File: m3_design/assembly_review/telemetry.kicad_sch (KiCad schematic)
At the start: 37 parts, among them J130 RADIO M0/M1/RXD/TXD/AUX/VCC/G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, J131 GPS 5V/GND/TX/RX, U14 AP63301WU-7, U15 TPS2553DBVR, U16 TPS259570DSGR

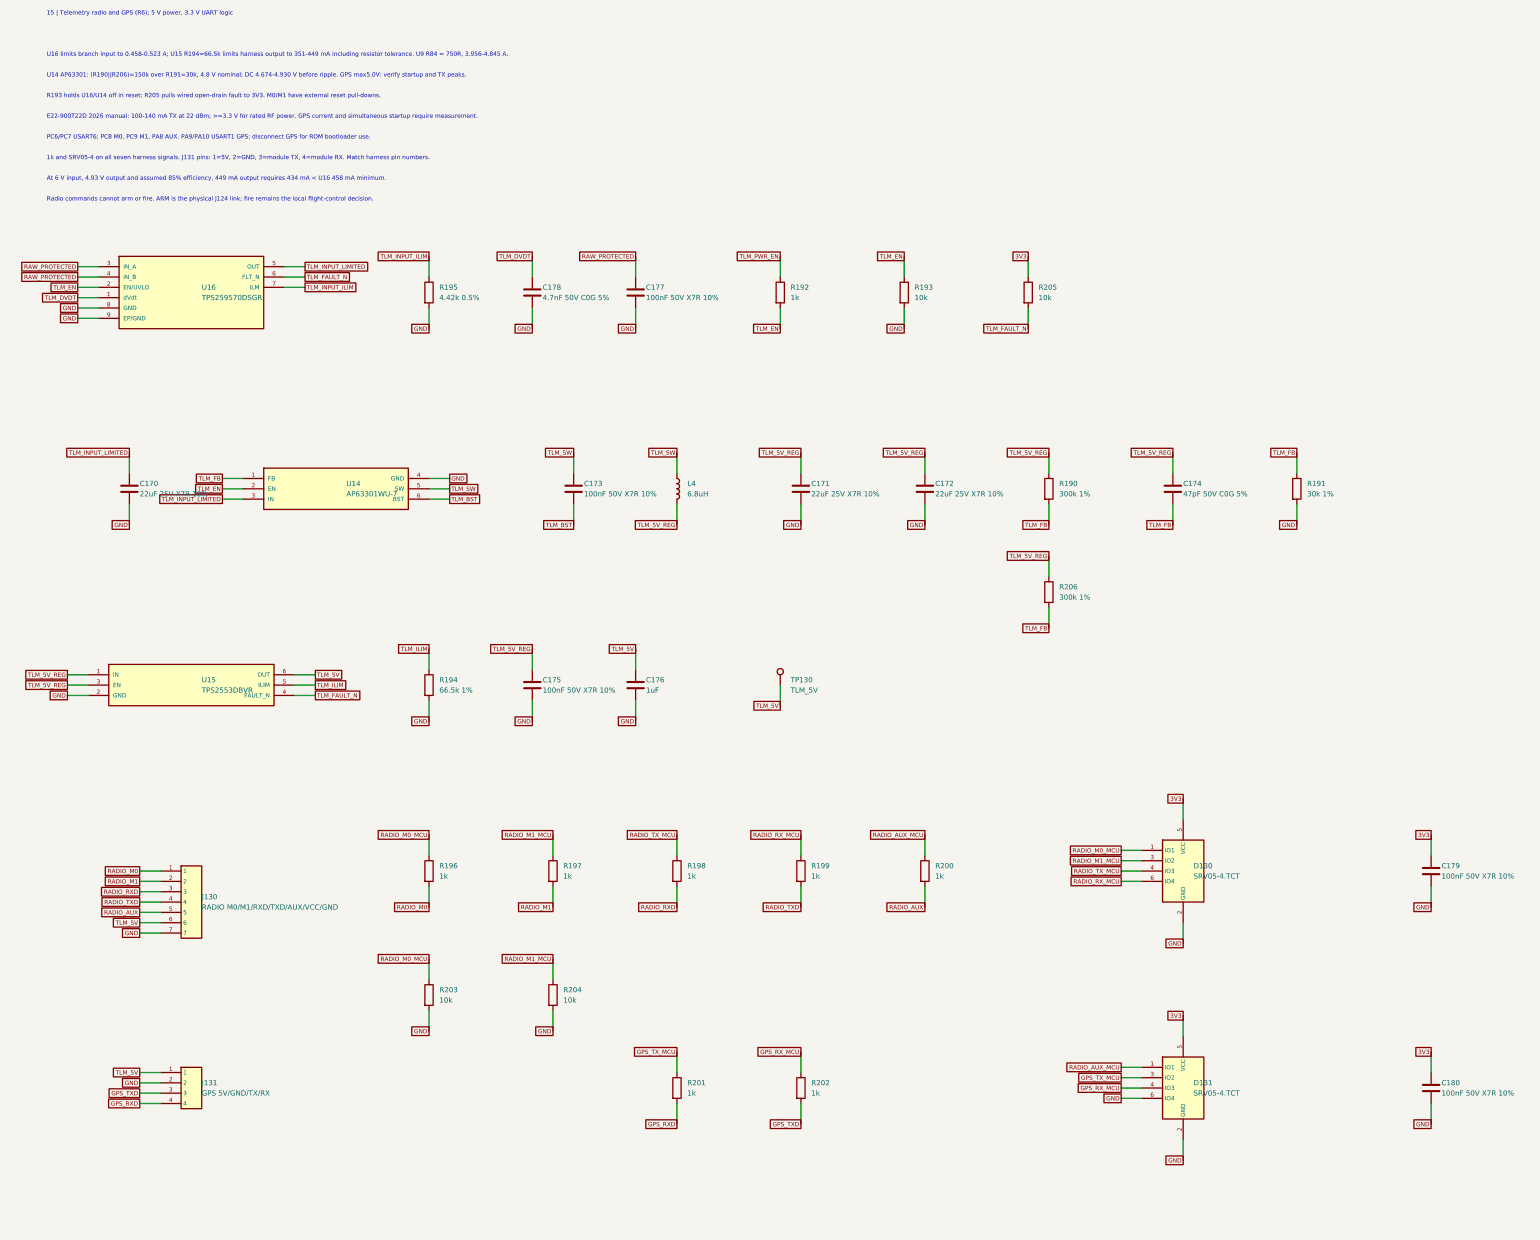
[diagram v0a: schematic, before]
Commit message: M3-ASSY-R7: on-board GNSS and LoRa radio, clean-routing gate, owner-accepted deviations
R7 replaces R6's external radio/GPS harness ports with an on-board u-blox
MAX-F10S (U30, MAX-M10S drop-in) and EBYTE E22-900MM22S SX1262 radio (U31)
in an RF strip at the aft end, each with an edge-launch SMA jack (J30 GNSS,
J31 RADIO), RF ESD, an antenna-bias current limiter and DNP tuning pads.
The board grows to 46 x 118 mm (R6 copper translated +18 mm).

- Schematic, parts and footprints: r7_sch.py, r7_parts.py
- Reproducible board build from the SHA-checked R6 board: r7_build.sh
  (r7_pcb, r7_route, r7_redraw, r7_rework, r7_hygiene, r7_polish, r7_post)
- Gate: check_r7.py (RF contract), route_check.py (clean routing, M2)
  in tools/check.sh; fit_check, cost and procurement updated for R7
- Eight independent review passes with skeptic verification; pass 8 on
  this board found 0 Critical / 0 Major
- Owner accepted the deviation list on 2026-10-18 (R7_VALIDATION), with
  the 7.7 A servo-feed copper rise accepted as estimated

Board SHA-256 c872a3d30509cccf5f78b64cde48ef722ee85c7be23c4848b07ce4082a852de3.
tools/check.sh: DRC 0, unconnected 0, parity 0, ERC 0; audit, silk,
R7 contract, routing hygiene (0 failing), actuator contract and fit OK.
Before ordering: consign U4 and get JLC's forward-rail confirmation.

Co-Authored-By: Claude Opus 5.5 <noreply@anthropic.com>
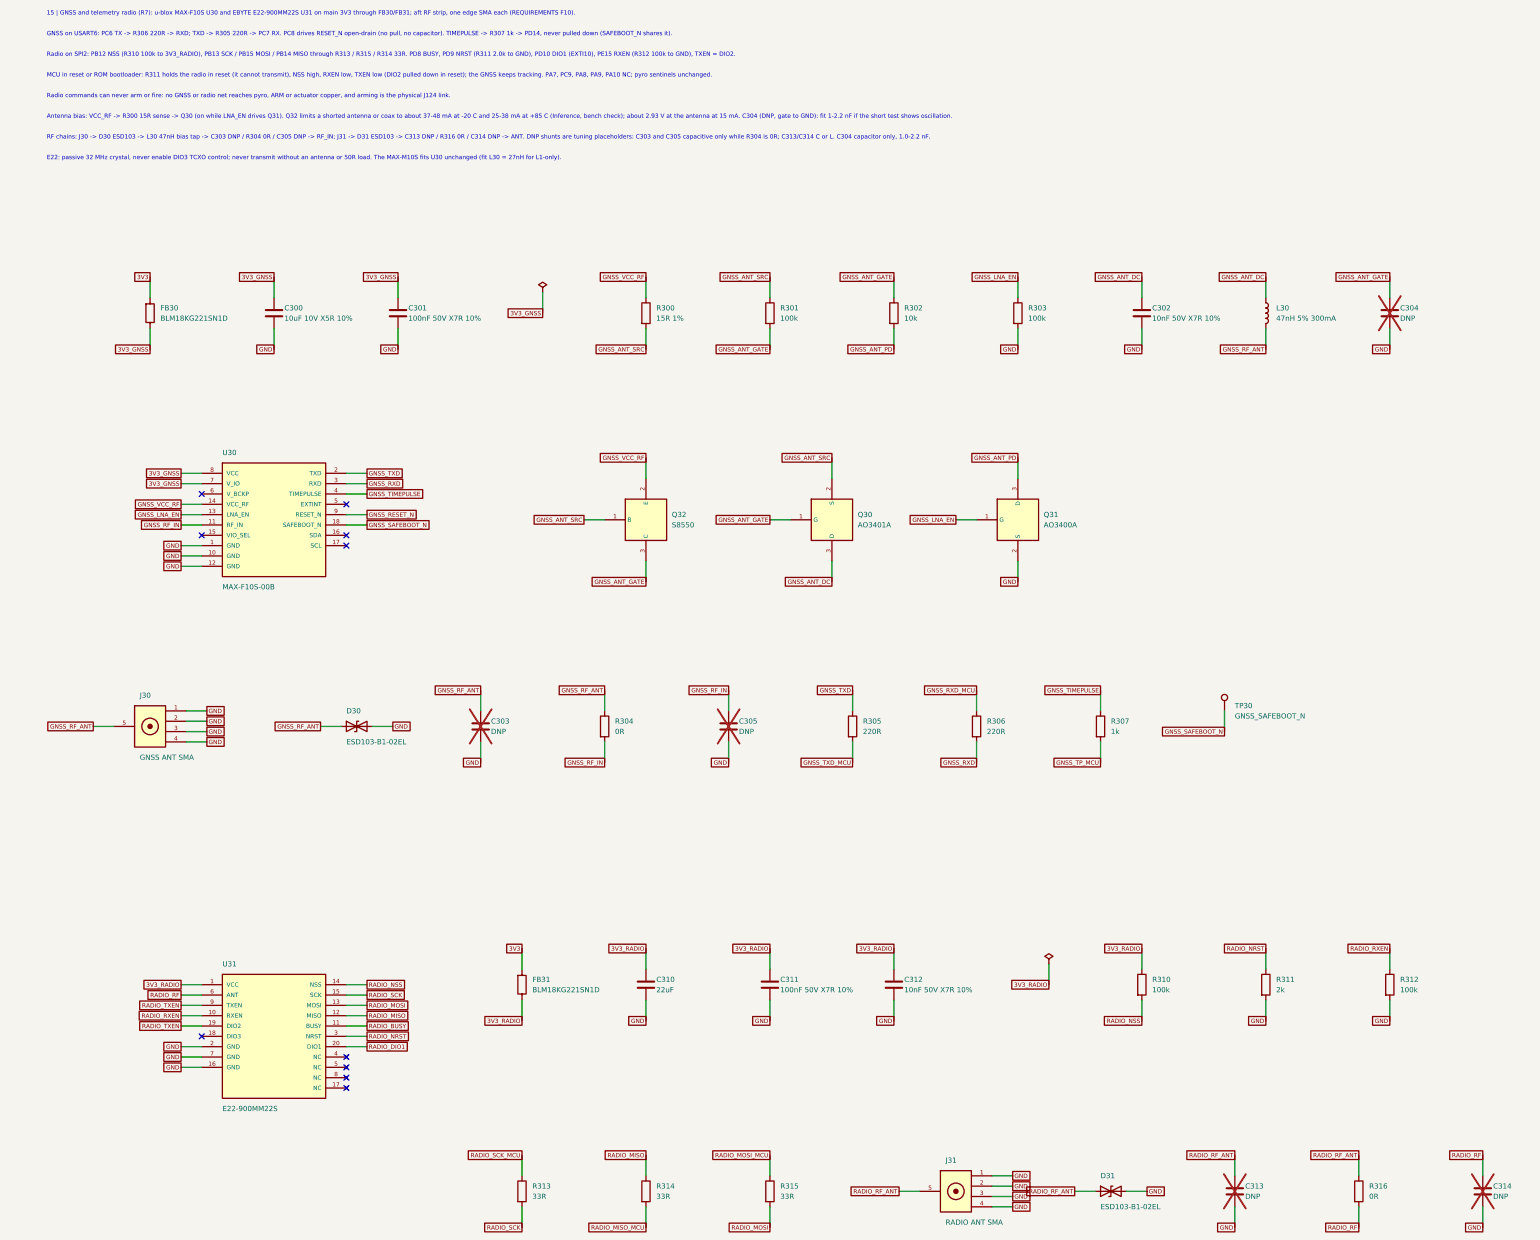
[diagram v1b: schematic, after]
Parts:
- removed C170, C171, C172: 22uF 25V X7R 10%, rocket:M3_GRM32_1210, symbol M3:C
- removed C173, C175, C177, C179, C180: 100nF 50V X7R 10%, rocket:C_0603_1608Metric, symbol M3:C
- removed C174: 47pF 50V C0G 5%, rocket:C_0603_1608Metric, symbol M3:C
- removed C176: 1uF, rocket:C0603, symbol M3:C
- removed C178: 4.7nF 50V C0G 5%, rocket:C_0603_1608Metric, symbol M3:C
- removed D130, D131: SRV05-4.TCT, rocket:SOT-23-6_L2.9-W1.6-P0.95-LS2.8-BL, symbol M3:SRV05_4
- removed J130: RADIO M0/M1/RXD/TXD/AUX/VCC/GND, rocket:M3_SH_BM07B_SRSS_TB, symbol M3:Conn_1x7
- removed J131: GPS 5V/GND/TX/RX, rocket:M3_SH_BM04B_SRSS_TB, symbol M3:Conn_1x4
- removed L4: 6.8uH, rocket:M3_SRP5030TA, symbol M3:L
- removed R190, R206: 300k 1%, rocket:R_0603_1608Metric, symbol M3:R
- removed R191: 30k 1%, rocket:R_0603_1608Metric, symbol M3:R
- removed R192, R196, R197, R198, R199, R200, R201, R202: 1k, rocket:R0402, symbol M3:R
- removed R193, R203, R204, R205: 10k, rocket:R0402, symbol M3:R
- removed R194: 66.5k 1%, rocket:R_0603_1608Metric, symbol M3:R
- removed R195: 4.42k 0.5%, rocket:R_0603_1608Metric, symbol M3:R
- removed TP130: TLM_5V, rocket:M3_TestPad_1.5, symbol M3:TestPoint
- removed U14: AP63301WU-7, rocket:M3_AP63200_TSOT26, symbol M3:CameraBuck
- removed U15: TPS2553DBVR, rocket:M3_TPS2553_DBV, symbol M3:USBCurrentLimit
- removed U16: TPS259570DSGR, rocket:M3_TPS2595_DSG, symbol M3:CameraEFuse
- added C300: 10uF 10V X5R 10%, rocket:C0603, symbol M3:C
- added C301, C311: 100nF 50V X7R 10%, rocket:C0402, symbol M3:C
- added C302, C312: 10nF 50V X7R 10%, rocket:C0402, symbol M3:C
- added C303, C304, C305, C313, C314: DNP, rocket:C0402_DNP, symbol M3:C
- added C310: 22uF, rocket:C0805, symbol M3:C
- added D30, D31: ESD103-B1-02EL, rocket:M3_TSLP_2_20, symbol M3:ESD_Bidir
- added FB30, FB31: BLM18KG221SN1D, rocket:M3_BLM18K_0603, symbol M3:FerriteBead
- added J30: GNSS ANT SMA, rocket:M3_SMA_KH_KE8_EDGE, symbol M3:SMA_Edge
- added J31: RADIO ANT SMA, rocket:M3_SMA_KH_KE8_EDGE, symbol M3:SMA_Edge
- added L30: 47nH 5% 300mA, rocket:M3_LQG15_0402, symbol M3:L
- added Q30: AO3401A, rocket:SOT-23-3_L2.9-W1.3-P1.90-LS2.4-BR, symbol M3:PMOS_SOT23
- added Q31: AO3400A, rocket:SOT-23-3_L2.9-W1.3-P1.90-LS2.4-BR, symbol M3:NMOS_SOT23
- added Q32: S8550, rocket:SOT-23-3_L2.9-W1.3-P1.90-LS2.4-BR, symbol M3:PNP_SOT23
- added R300: 15R 1%, rocket:R_0603_1608Metric, symbol M3:R
- added R301, R303, R310, R312: 100k, rocket:R0402, symbol M3:R
- added R302: 10k, rocket:R0402, symbol M3:R
- added R304, R316: 0R, rocket:R0402, symbol M3:R
- added R305, R306: 220R, rocket:R0402, symbol M3:R
- added R307: 1k, rocket:R0402, symbol M3:R
- added R311: 2k, rocket:R0402, symbol M3:R
- added R313, R314, R315: 33R, rocket:R0402, symbol M3:R
- added TP30: GNSS_SAFEBOOT_N, rocket:M3_TestPad_1.5, symbol M3:TestPoint
- added U30: MAX-F10S-00B, rocket:M3_MAX_F10S_LCC18, symbol M3:MAX_F10S
- added U31: E22-900MM22S, rocket:M3_E22_900MM22S, symbol M3:E22_900MM22S
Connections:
- net 3V3: now also FB30.1, FB31.1
- net GND: now also C300.2, C301.2, C302.2, C303.2, C304.2, C305.2, C310.2, C311.2, C312.2, C313.2, C314.2, D30.2 (A2), D31.2 (A2), J30.1 (SH), J30.2 (SH), J30.3 (SH), J30.4 (SH), J31.1 (SH), J31.2 (SH), J31.3 (SH), J31.4 (SH), Q31.2 (S), R303.2, R311.2, R312.2, U30.1 (GND), U30.10 (GND), U30.12 (GND), U31.16 (GND), U31.2 (GND), U31.7 (GND)
- new net 3V3_GNSS: C300.1, C301.1, FB30.2, U30.7 (V_IO), U30.8 (VCC)
- new net 3V3_RADIO: C310.1, C311.1, C312.1, FB31.2, R310.1, U31.1 (VCC)
- new net GNSS_ANT_DC: C302.1, L30.1, Q30.3 (D)
- new net GNSS_ANT_GATE: C304.1, Q30.1 (G), Q32.3 (C), R301.2, R302.1
- new net GNSS_ANT_PD: Q31.3 (D), R302.2
- new net GNSS_ANT_SRC: Q30.2 (S), Q32.1 (B), R300.2, R301.1
- new net GNSS_LNA_EN: Q31.1 (G), R303.1, U30.13 (LNA_EN)
- new net GNSS_RESET_N: U30.9 (RESET_N)
- new net GNSS_RF_ANT: C303.1, D30.1 (A1), J30.5 (SIG), L30.2, R304.1
- new net GNSS_RF_IN: C305.1, R304.2, U30.11 (RF_IN)
- new net GNSS_RXD: R306.2, U30.3 (RXD)
- new net GNSS_RXD_MCU: R306.1
- new net GNSS_SAFEBOOT_N: TP30.1, U30.18 (SAFEBOOT_N)
- new net GNSS_TIMEPULSE: R307.1, U30.4 (TIMEPULSE)
- new net GNSS_TP_MCU: R307.2
- new net GNSS_TXD: R305.1, U30.2 (TXD)
- new net GNSS_TXD_MCU: R305.2
- new net GNSS_VCC_RF: Q32.2 (E), R300.1, U30.14 (VCC_RF)
- new net RADIO_BUSY: U31.11 (BUSY)
- new net RADIO_DIO1: U31.20 (DIO1)
- new net RADIO_MISO: R314.1, U31.12 (MISO)
- new net RADIO_MISO_MCU: R314.2
- new net RADIO_MOSI: R315.2, U31.13 (MOSI)
- new net RADIO_MOSI_MCU: R315.1
- new net RADIO_NRST: R311.1, U31.3 (NRST)
- new net RADIO_NSS: R310.2, U31.14 (NSS)
- new net RADIO_RF: C314.1, R316.2, U31.6 (ANT)
- new net RADIO_RF_ANT: C313.1, D31.1 (A1), J31.5 (SIG), R316.1
- new net RADIO_RXEN: R312.1, U31.10 (RXEN)
- new net RADIO_SCK: R313.2, U31.15 (SCK)
- new net RADIO_SCK_MCU: R313.1
- new net RADIO_TXEN: U31.19 (DIO2), U31.9 (TXEN)
- no-connect marks 0 -> 10
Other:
- note added: "15 | GNSS and telemetry radio (R7): u-blox MAX-F10S U30 and EBYTE E22-900MM22S U31 on main 3V3 through FB30/FB31; aft RF strip, one edge SMA each (REQUIREMENTS F10)."
- note added: "Antenna bias: VCC_RF -> R300 15R sense -> Q30 (on while LNA_EN drives Q31). Q32 limits a shorted antenna or coax to about 37-48 mA at -20 C and 25-38 mA at +85 C (Inference, bench check); about 2.93 V at the antenna at 15 mA. C304 (DNP, gate to GND): fit 1-2.2 nF if the short test shows oscillation."
- note added: "E22: passive 32 MHz crystal, never enable DIO3 TCXO control; never transmit without an antenna or 50R load. The MAX-M10S fits U30 unchanged (fit L30 = 27nH for L1-only)."
- note added: "GNSS on USART6: PC6 TX -> R306 220R -> RXD; TXD -> R305 220R -> PC7 RX. PC8 drives RESET_N open-drain (no pull, no capacitor). TIMEPULSE -> R307 1k -> PD14, never pulled down (SAFEBOOT_N shares it)."
- note added: "MCU in reset or ROM bootloader: R311 holds the radio in reset (it cannot transmit), NSS high, RXEN low, TXEN low (DIO2 pulled down in reset); the GNSS keeps tracking. PA7, PC9, PA8, PA9, PA10 NC; pyro sentinels unchanged."
- note added: "RF chains: J30 -> D30 ESD103 -> L30 47nH bias tap -> C303 DNP / R304 0R / C305 DNP -> RF_IN; J31 -> D31 ESD103 -> C313 DNP / R316 0R / C314 DNP -> ANT. DNP shunts are tuning placeholders: C303 and C305 capacitive only while R304 is 0R; C313/C314 C or L. C304 capacitor only, 1.0-2.2 nF."
- note added: "Radio commands can never arm or fire: no GNSS or radio net reaches pyro, ARM or actuator copper, and arming is the physical J124 link."
- note added: "Radio on SPI2: PB12 NSS (R310 100k to 3V3_RADIO), PB13 SCK / PB15 MOSI / PB14 MISO through R313 / R315 / R314 33R. PD8 BUSY, PD9 NRST (R311 2.0k to GND), PD10 DIO1 (EXTI10), PE15 RXEN (R312 100k to GND), TXEN = DIO2."
- note removed: "15 | Telemetry radio and GPS (R6); 5 V power, 3.3 V UART logic"
- note removed: "1k and SRV05-4 on all seven harness signals. J131 pins: 1=5V, 2=GND, 3=module TX, 4=module RX. Match harness pin numbers."
- note removed: "At 6 V input, 4.93 V output and assumed 85% efficiency, 449 mA output requires 434 mA < U16 458 mA minimum."
- note removed: "E22-900T22D 2026 manual: 100-140 mA TX at 22 dBm; >=3.3 V for rated RF power. GPS current and simultaneous startup require measurement."
- note removed: "PC6/PC7 USART6; PC8 M0, PC9 M1, PA8 AUX. PA9/PA10 USART1 GPS; disconnect GPS for ROM bootloader use."
- note removed: "R193 holds U16/U14 off in reset; R205 pulls wired open-drain fault to 3V3. M0/M1 have external reset pull-downs."
- note removed: "Radio commands cannot arm or fire. ARM is the physical J124 link; fire remains the local flight-control decision."
- note removed: "U14 AP63301: (R190||R206)=150k over R191=30k, 4.8 V nominal; DC 4.674-4.930 V before ripple. GPS max5.0V: verify startup and TX peaks."
- note removed: "U16 limits branch input to 0.458-0.523 A; U15 R194=66.5k limits harness output to 351-449 mA including resistor tolerance. U9 R84 = 750R, 3.956-4.845 A."
- company: Single-board M3 candidate; telemetry port, not bench-verified -> Single-board M3 candidate; on-board GNSS and radio, not bench-verified
- title: 15 | Telemetry radio and GPS port -> 15 | GNSS and telemetry radio (R7)
